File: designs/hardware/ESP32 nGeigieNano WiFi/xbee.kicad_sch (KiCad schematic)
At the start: 9 parts, among them SW1 TACT-SWITCH, SW2 SWITCH_INV, U1 ESP32S, U2 XBEE-socket

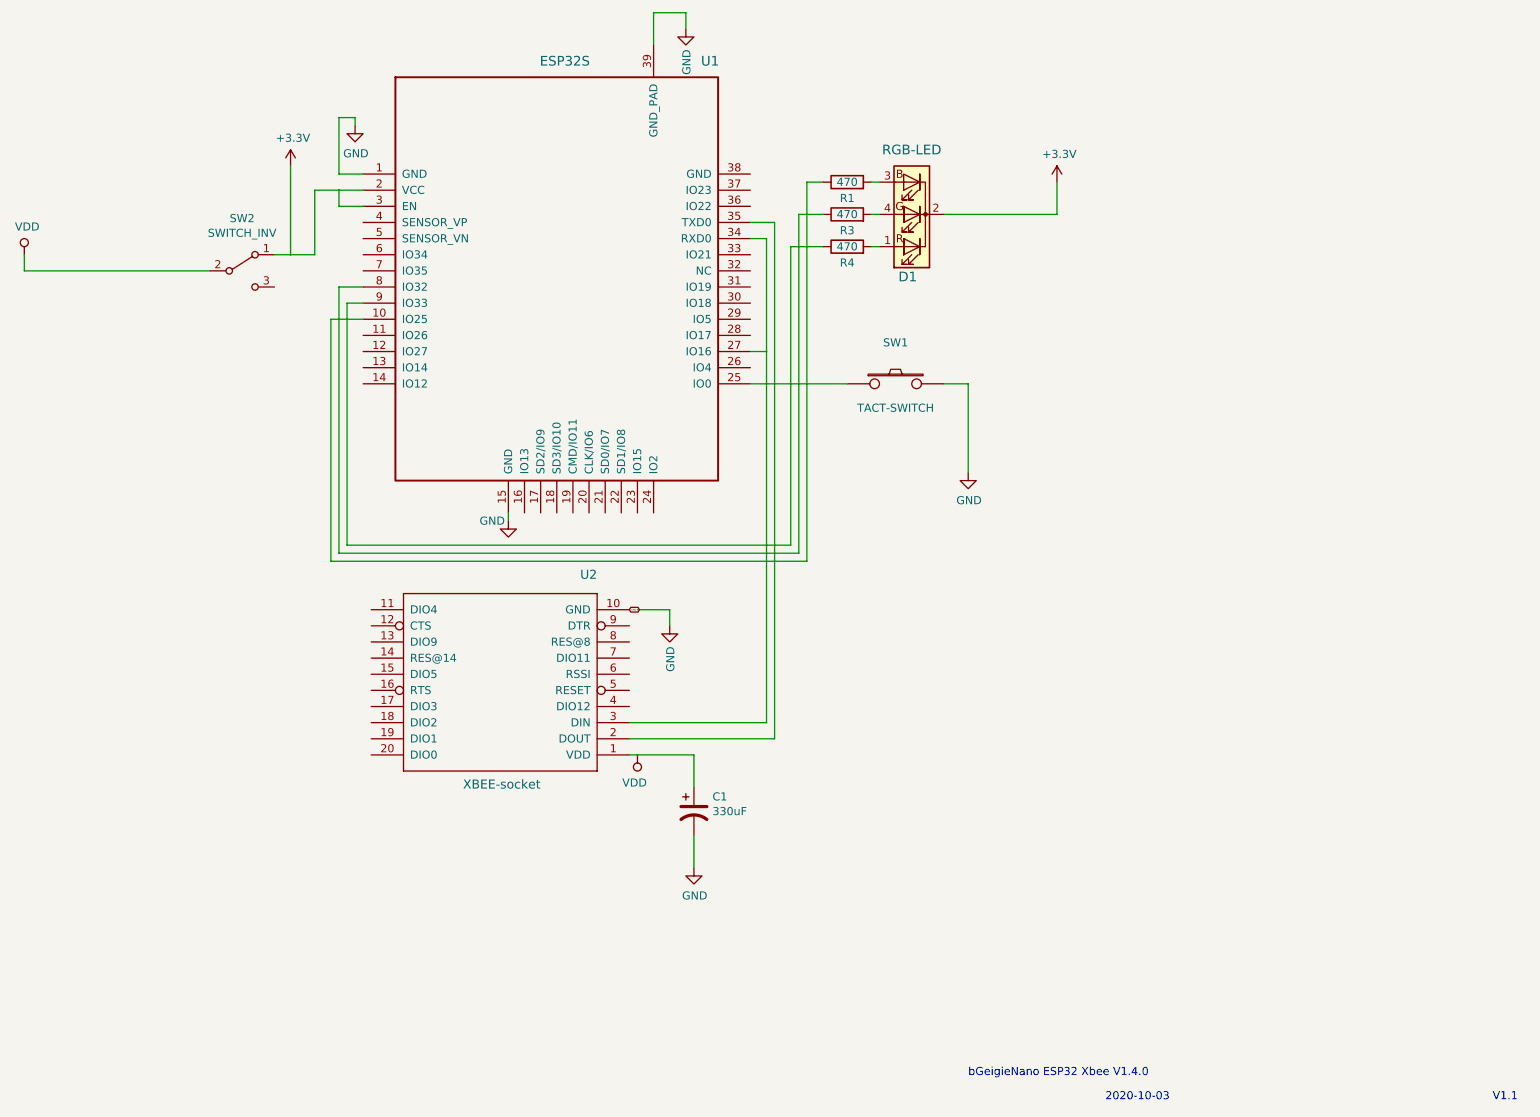
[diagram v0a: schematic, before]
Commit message: Added bGigeiCast files to be implemented
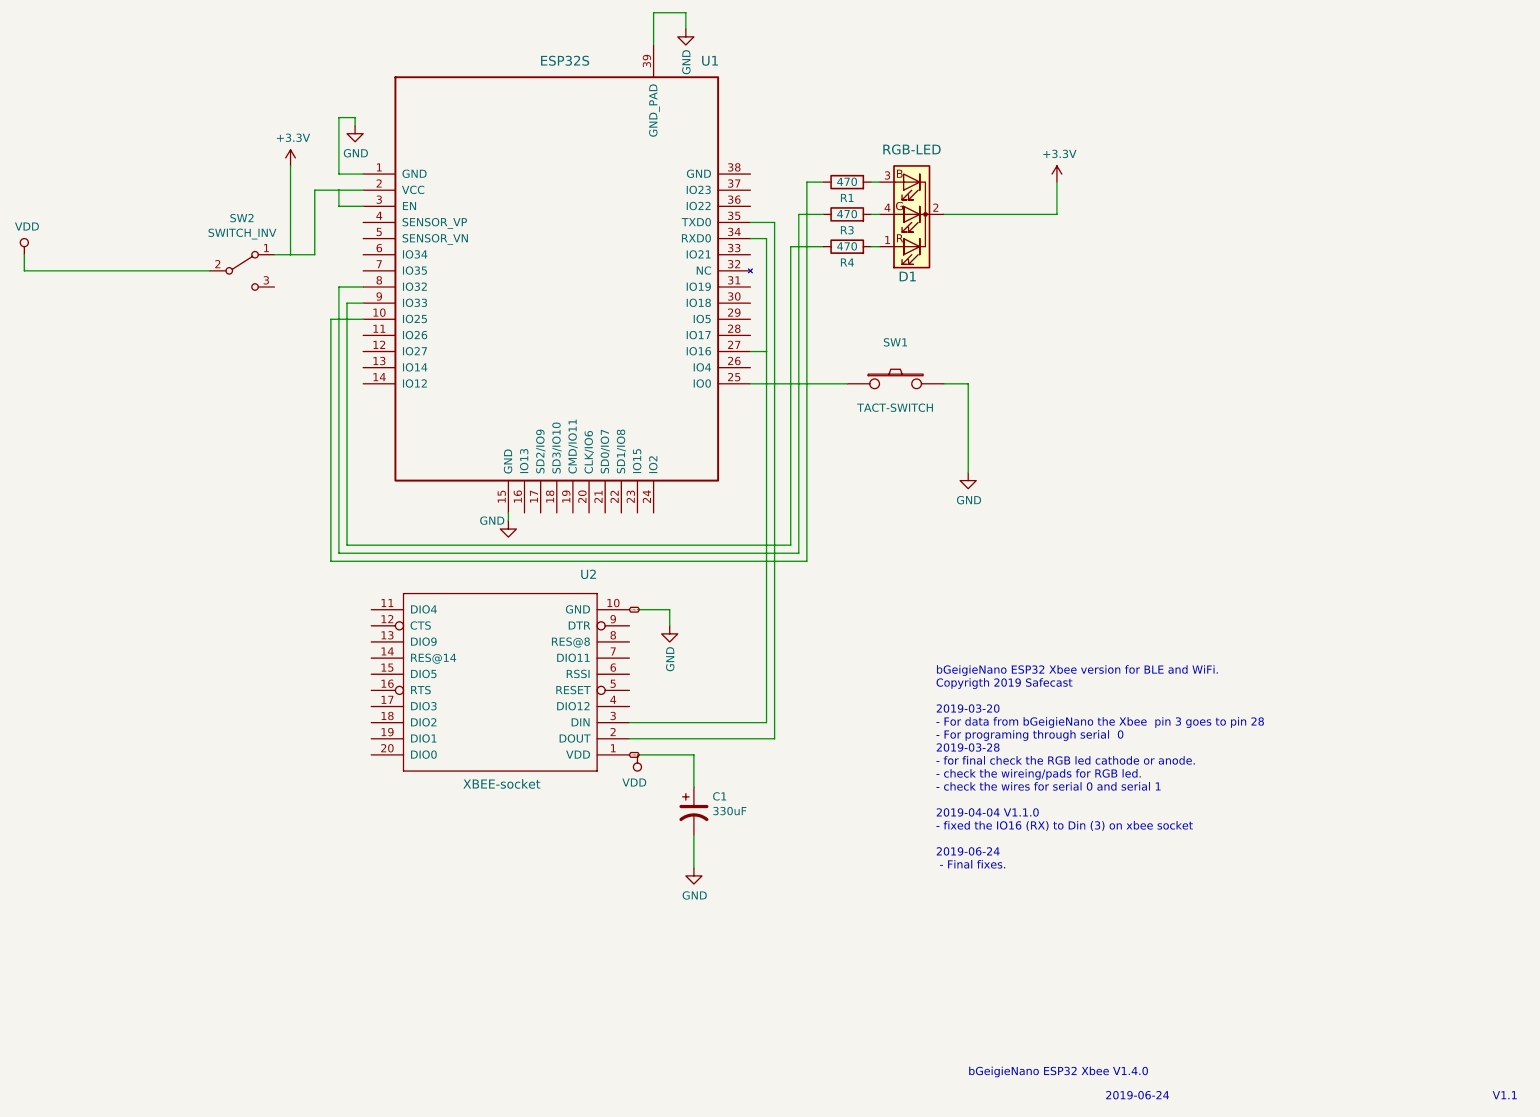
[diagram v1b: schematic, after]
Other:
- note added: "2019-06-24"
- note added: "bGeigieNano ESP32 Xbee version for BLE and WiFi. Copyrigth 2019 Safecast 2019-03-20 - For data from bGeigieNano the Xbee pin 3 goes to pin 28 - For programing through serial 0 2019-03-28 - for final check the RGB led cathode or anode. - check the wireing/pads for RGB led. - check the wires for serial 0 and serial 1 2019-04-04 V1.1.0 - fixed the IO16 (RX) to Din (3) on xbee socket 2019-06-24 - Fin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"
- note removed: "2020-10-03"
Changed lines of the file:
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@@
-(kicad_sch (version 20200828) (generator eeschema)
-  (page 1 1)
+(kicad_sch (version 20210126) (generator eeschema)
   (paper "A4")
-  (junction (at 80.01 60.96) (diameter 0.2591) (color 0 0 0 0))
-  (junction (at 87.63 50.8) (diameter 0.2591) (color 0 0 0 0))
-  (junction (at 134.62 139.7) (diameter 0.2591) (color 0 0 0 0))
-  (junction (at 154.94 76.2) (diameter 0.2591) (color 0 0 0 0))
+  (junction (at 80.01 60.96) (diameter 0.259) (color 0 0 0 0))
+  (junction (at 87.63 50.8) (diameter 0.259) (color 0 0 0 0))
+  (junction (at 154.94 76.2) (diameter 0.259) (color 0 0 0 0))
   (wire (pts (xy 38.1 63.5) (xy 38.1 60.96))
     (stroke (width 0) (type solid) (color 0 0 0 0))
@@
     (stroke (width 0) (type solid) (color 0 0 0 0))
   )
-  (wire (pts (xy 133.35 139.7) (xy 134.62 139.7))
-    (stroke (width 0) (type solid) (color 0 0 0 0))
-  )
   (wire (pts (xy 134.62 116.84) (xy 139.7 116.84))
     (stroke (width 0) (type solid) (color 0 0 0 0))
@@
   (wire (pts (xy 200.66 54.61) (xy 200.66 49.53))
     (stroke (width 0) (type solid) (color 0 0 0 0))
+  )
+  (text "bGeigieNano ESP32 Xbee version for BLE and WiFi.\nCopyrigth 2019 Safecast\n\n2019-03-20\n- For data from bGeigieNano the Xbee  pin 3 goes to pin 28\n- For programing through serial  0\n2019-03-28\n- for final check the RGB led cathode or anode.\n- check the wireing/pads for RGB led.\n- check the wires for serial 0 and serial 1\n\n2019-04-04 V1.1.0 \n- fixed the IO16 (RX) to Din (3) on xbee socket\n\n2019-06-24\n - Final fixes.\n\n"
+    (at 181.61 160.02 0)
+    (effects (font (size 1.27 1.27)) (justify left bottom))
   )
   (text "bGeigieNano ESP32 Xbee V1.4.0" (at 186.69 190.5 0)
     (effects (font (size 1.27 1.27)) (justify left bottom))
   )
-  (text "2020-10-03" (at 208.28 194.31 0)
+  (text "2019-06-24" (at 208.28 194.31 0)
     (effects (font (size 1.27 1.27)) (justify left bottom))
   )
@@
   (global_label "GND" (shape bidirectional) (at 133.35 116.84 0)
     (effects (font (size 0.254 0.254)) (justify left))
+    (property "Intersheet References" "${INTERSHEET_REFS}" (id 0) (at 0 0 0)
+      (effects (font (size 1.27 1.27)) hide)
+    )
+  )
+  (global_label "VDD" (shape bidirectional) (at 133.35 139.7 0)
+    (effects (font (size 0.254 0.254)) (justify left))
+    (property "Intersheet References" "${INTERSHEET_REFS}" (id 0) (at 0 0 0)
+      (effects (font (size 1.27 1.27)) hide)
+    )
   )
   (symbol (lib_id "power:VDD") (at 38.1 60.96 0) (unit 1)
@@
       (effects (font (size 1.27 1.27)) hide)
     )
+    (pin "1")
   )
   (symbol (lib_id "power:VDD") (at 134.62 139.7 180) (unit 1)
@@
       (effects (font (size 1.27 1.27)) hide)
     )
+    (pin "1")
   )
   (symbol (lib_id "power:+3.3V") (at 80.01 46.99 0) (unit 1)
@@
       (effects (font (size 1.27 1.27)) hide)
     )
+    (pin "1")
   )
   (symbol (lib_id "power:+3.3V") (at 200.66 49.53 0) (unit 1)
@@
       (effects (font (size 1.27 1.27)) hide)
     )
+    (pin "1")
   )
   (symbol (lib_id "xbee-rescue:GND-kicad_project_geiger-cache") (at 90.17 40.64 0) (unit 1)
@@
     (property "Footprint" "" (id 2) (at 90.17 40.64 0))
     (property "Datasheet" "" (id 3) (at 90.17 40.64 0))
+    (pin "1")
   )
   (symbol (lib_id "xbee-rescue:GND-kicad_project_geiger-cache") (at 114.3 102.87 0) (unit 1)
@@
     (property "Footprint" "" (id 2) (at 114.3 102.87 0))
     (property "Datasheet" "" (id 3) (at 114.3 102.87 0))
+    (pin "1")
   )
   (symbol (lib_id "xbee-rescue:GND-kicad_project_geiger-cache") (at 139.7 119.38 0) (unit 1)
@@
     (property "Footprint" "" (id 2) (at 139.7 119.38 0))
     (property "Datasheet" "" (id 3) (at 139.7 119.38 0))
+    (pin "1")
   )
   (symbol (lib_id "xbee-rescue:GND-kicad_project_geiger-cache") (at 142.24 25.4 0) (unit 1)
@@
     (property "Footprint" "" (id 2) (at 142.24 25.4 0))
     (property "Datasheet" "" (id 3) (at 142.24 25.4 0))
+    (pin "1")
   )
   (symbol (lib_id "xbee-rescue:GND-kicad_project_geiger-cache") (at 143.51 157.48 0) (unit 1)
@@
     (property "Footprint" "" (id 2) (at 143.51 157.48 0))
     (property "Datasheet" "" (id 3) (at 143.51 157.48 0))
+    (pin "1")
   )
   (symbol (lib_id "xbee-rescue:GND-kicad_project_geiger-cache") (at 186.69 95.25 0) (unit 1)
@@
     (property "Footprint" "" (id 2) (at 186.69 95.25 0))
     (property "Datasheet" "" (id 3) (at 186.69 95.25 0))
+    (pin "1")
   )
   (symbol (lib_id "xbee-rescue:R-device") (at 167.64 49.53 90) (unit 1)
@@
       (effects (font (size 1.27 1.27)) hide)
     )
+    (pin "1")
+    (pin "2")
   )
   (symbol (lib_id "xbee-rescue:R-device") (at 167.64 54.61 90) (unit 1)
@@
       (effects (font (size 1.27 1.27)) hide)
     )
+    (pin "1")
+    (pin "2")
   )
   (symbol (lib_id "xbee-rescue:R-device") (at 167.64 59.69 90) (unit 1)
@@
       (effects (font (size 1.27 1.27)) hide)
     )
+    (pin "1")
+    (pin "2")
   )
   (symbol (lib_id "xbee-rescue:CP1-kicad_project_geiger-cache") (at 143.51 148.59 0) (unit 1)
@@
     )
     (property "Datasheet" "" (id 3) (at 143.51 148.59 0))
+    (pin "1")
+    (pin "2")
   )
   (symbol (lib_id "xbee-rescue:TACT-SWITCH-tinkerforge") (at 175.26 81.28 0) (unit 1)
@@
       (effects (font (size 1.524 1.524)))
     )
+    (pin "1")
+    (pin "2")
   )
   (symbol (lib_id "Switch:SW_SPDT") (at 72.39 63.5 0) (unit 1)
@@
     )
     (property "Datasheet" "" (id 3) (at 72.39 63.5 0))
+    (pin "1")
+    (pin "2")
+    (pin "3")
   )
   (symbol (lib_id "xbee-rescue:LED_RCBG-device") (at 177.8 54.61 180) (unit 1)
@@
       (effects (font (size 1.524 1.524)))
     )
+    (pin "1")
+    (pin "2")
+    (pin "3")
+    (pin "4")
   )
   (symbol (lib_id "xbee-eagle-import:XBEE-1B2") (at 113.03 129.54 180) (unit 1)
@@
       (effects (font (size 1.27 1.27)) hide)
     )
+    (pin "1")
+    (pin "10")
+    (pin "11")
+    (pin "12")
+    (pin "13")
+    (pin "14")
+    (pin "15")
+    (pin "16")
+    (pin "17")
+    (pin "18")
+    (pin "19")
+    (pin "2")
+    (pin "20")
+    (pin "3")
+    (pin "4")
+    (pin "5")
+    (pin "6")
+    (pin "7")
+    (pin "8")
+    (pin "9")
   )
   (symbol (lib_id "xbee-rescue:ESP32S-espressif-xess") (at 91.44 48.26 0) (unit 1)
@@
       (effects (font (size 1.27 1.27)) hide)
     )
+    (pin "1")
+    (pin "10")
+    (pin "11")
+    (pin "12")
+    (pin "13")
+    (pin "14")
+    (pin "15")
+    (pin "16")
+    (pin "17")
+    (pin "18")
+    (pin "19")
+    (pin "2")
+    (pin "20")
+    (pin "21")
+    (pin "22")
+    (pin "23")
+    (pin "24")
+    (pin "25")
+    (pin "26")
+    (pin "27")
+    (pin "28")
+    (pin "29")
+    (pin "3")
+    (pin "30")
+    (pin "31")
+    (pin "32")
+    (pin "33")
+    (pin "34")
+    (pin "35")
+    (pin "36")
+    (pin "37")
+    (pin "38")
+    (pin "39")
+    (pin "4")
+    (pin "5")
+    (pin "6")
+    (pin "7")
+    (pin "8")
+    (pin "9")
+  )
+  (sheet_instances
+    (path "/" (page "1"))
   )
   (symbol_instances
